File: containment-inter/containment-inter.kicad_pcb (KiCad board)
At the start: 2 copper layers, 25.4 x 25.4 mm, 1 part

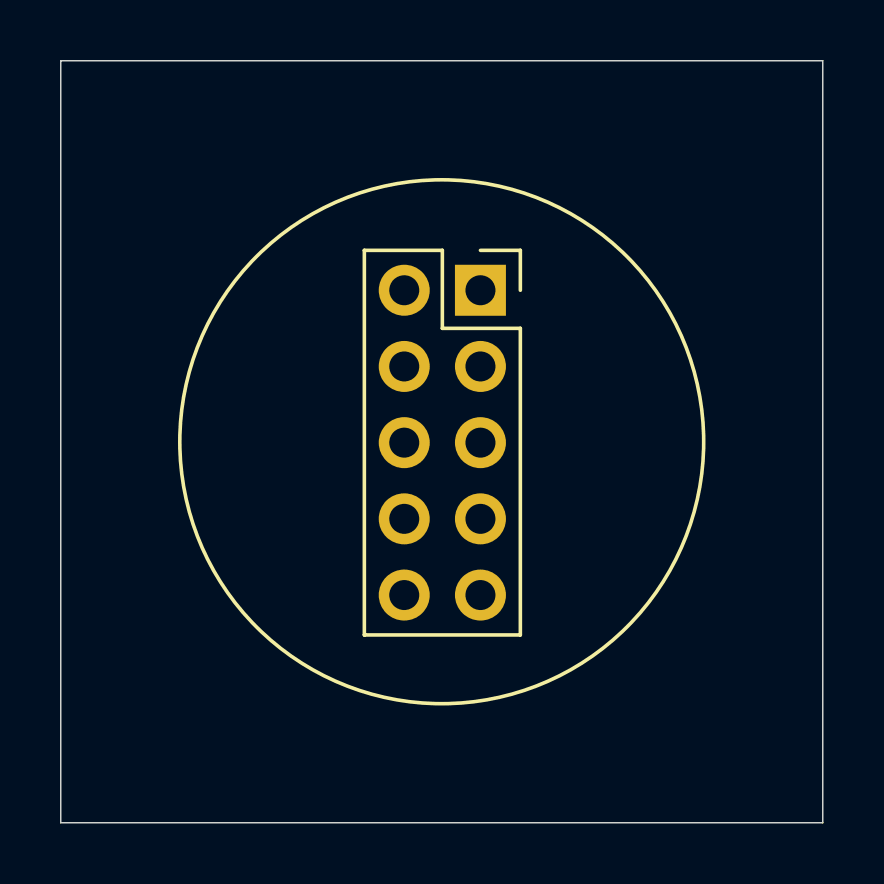
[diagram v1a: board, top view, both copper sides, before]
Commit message: more lcsc, redo a lot of inner containment
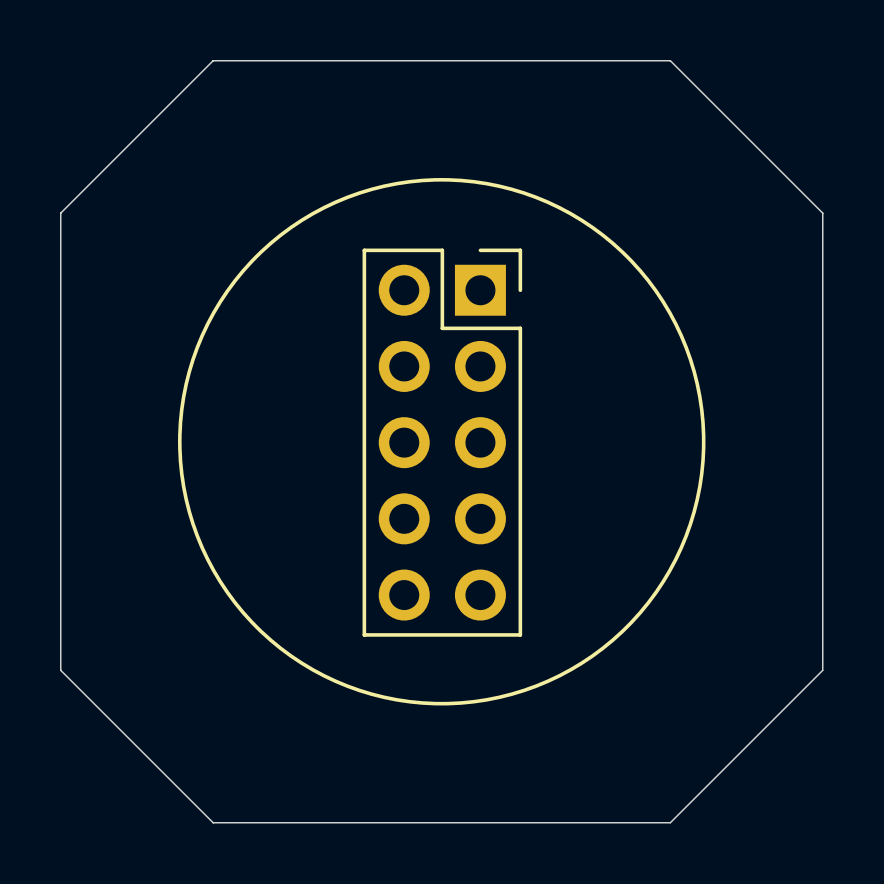
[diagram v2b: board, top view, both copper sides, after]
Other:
- outline, holes or cut-outs redrawn
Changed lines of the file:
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@@
-(kicad_pcb (version 20171130) (host pcbnew 5.1.6+dfsg1-1)
+(kicad_pcb (version 20171130) (host pcbnew 5.1.8+dfsg1-1+b1)
   (general
     (thickness 1.6)
-    (drawings 5)
+    (drawings 9)
     (tracks 0)
     (zones 0)
@@
       (effects (font (size 1 1) (thickness 0.15)))
     )
+    (fp_line (start -3.81 -1.27) (end 0.27 -1.27) (layer F.Fab) (width 0.1))
+    (fp_line (start 0.27 -1.27) (end 1.27 -0.27) (layer F.Fab) (width 0.1))
+    (fp_line (start 1.27 -0.27) (end 1.27 11.43) (layer F.Fab) (width 0.1))
+    (fp_line (start 1.27 11.43) (end -3.81 11.43) (layer F.Fab) (width 0.1))
+    (fp_line (start -3.81 11.43) (end -3.81 -1.27) (layer F.Fab) (width 0.1))
+    (fp_line (start -3.87 -1.33) (end -1.27 -1.33) (layer F.SilkS) (width 0.12))
+    (fp_line (start -3.87 -1.33) (end -3.87 11.49) (layer F.SilkS) (width 0.12))
+    (fp_line (start -3.87 11.49) (end 1.33 11.49) (layer F.SilkS) (width 0.12))
+    (fp_line (start 1.33 1.27) (end 1.33 11.49) (layer F.SilkS) (width 0.12))
+    (fp_line (start -1.27 1.27) (end 1.33 1.27) (layer F.SilkS) (width 0.12))
+    (fp_line (start -1.27 -1.33) (end -1.27 1.27) (layer F.SilkS) (width 0.12))
+    (fp_line (start 1.33 -1.33) (end 1.33 0) (layer F.SilkS) (width 0.12))
+    (fp_line (start 0 -1.33) (end 1.33 -1.33) (layer F.SilkS) (width 0.12))
+    (fp_line (start -4.34 -1.8) (end 1.76 -1.8) (layer F.CrtYd) (width 0.05))
+    (fp_line (start 1.76 -1.8) (end 1.76 11.9) (layer F.CrtYd) (width 0.05))
+    (fp_line (start 1.76 11.9) (end -4.34 11.9) (layer F.CrtYd) (width 0.05))
     (fp_line (start -4.34 11.9) (end -4.34 -1.8) (layer F.CrtYd) (width 0.05))
-    (fp_line (start 1.76 11.9) (end -4.34 11.9) (layer F.CrtYd) (width 0.05))
-    (fp_line (start 1.76 -1.8) (end 1.76 11.9) (layer F.CrtYd) (width 0.05))
-    (fp_line (start -4.34 -1.8) (end 1.76 -1.8) (layer F.CrtYd) (width 0.05))
-    (fp_line (start 0 -1.33) (end 1.33 -1.33) (layer F.SilkS) (width 0.12))
-    (fp_line (start 1.33 -1.33) (end 1.33 0) (layer F.SilkS) (width 0.12))
-    (fp_line (start -1.27 -1.33) (end -1.27 1.27) (layer F.SilkS) (width 0.12))
-    (fp_line (start -1.27 1.27) (end 1.33 1.27) (layer F.SilkS) (width 0.12))
-    (fp_line (start 1.33 1.27) (end 1.33 11.49) (layer F.SilkS) (width 0.12))
-    (fp_line (start -3.87 11.49) (end 1.33 11.49) (layer F.SilkS) (width 0.12))
-    (fp_line (start -3.87 -1.33) (end -3.87 11.49) (layer F.SilkS) (width 0.12))
-    (fp_line (start -3.87 -1.33) (end -1.27 -1.33) (layer F.SilkS) (width 0.12))
-    (fp_line (start -3.81 11.43) (end -3.81 -1.27) (layer F.Fab) (width 0.1))
-    (fp_line (start 1.27 11.43) (end -3.81 11.43) (layer F.Fab) (width 0.1))
-    (fp_line (start 1.27 -0.27) (end 1.27 11.43) (layer F.Fab) (width 0.1))
-    (fp_line (start 0.27 -1.27) (end 1.27 -0.27) (layer F.Fab) (width 0.1))
-    (fp_line (start -3.81 -1.27) (end 0.27 -1.27) (layer F.Fab) (width 0.1))
     (fp_text user %R (at 1 5 90) (layer F.Fab)
       (effects (font (size 1 1) (thickness 0.15)))
@@
     )
   )
+  (gr_line (start 182.88 121.92) (end 187.96 127) (layer Edge.Cuts) (width 0.05))
+  (gr_line (start 167.64 121.92) (end 162.56 127) (layer Edge.Cuts) (width 0.05))
+  (gr_line (start 167.64 147.32) (end 162.56 142.24) (layer Edge.Cuts) (width 0.05))
+  (gr_line (start 187.96 142.24) (end 182.88 147.32) (layer Edge.Cuts) (width 0.05))
   (gr_circle (center 175.26 134.62) (end 183.99125 134.62) (layer F.SilkS) (width 0.12))
-  (gr_line (start 162.56 147.32) (end 162.56 121.92) (layer Edge.Cuts) (width 0.05))
-  (gr_line (start 187.96 147.32) (end 162.56 147.32) (layer Edge.Cuts) (width 0.05))
-  (gr_line (start 187.96 121.92) (end 187.96 147.32) (layer Edge.Cuts) (width 0.05))
-  (gr_line (start 162.56 121.92) (end 187.96 121.92) (layer Edge.Cuts) (width 0.05))
+  (gr_line (start 162.56 142.24) (end 162.56 127) (layer Edge.Cuts) (width 0.05))
+  (gr_line (start 182.88 147.32) (end 167.64 147.32) (layer Edge.Cuts) (width 0.05))
+  (gr_line (start 187.96 127) (end 187.96 142.24) (layer Edge.Cuts) (width 0.05))
+  (gr_line (start 167.64 121.92) (end 182.88 121.92) (layer Edge.Cuts) (width 0.05))
 )
